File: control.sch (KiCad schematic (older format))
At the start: 1 part, among them J4 ProMicro

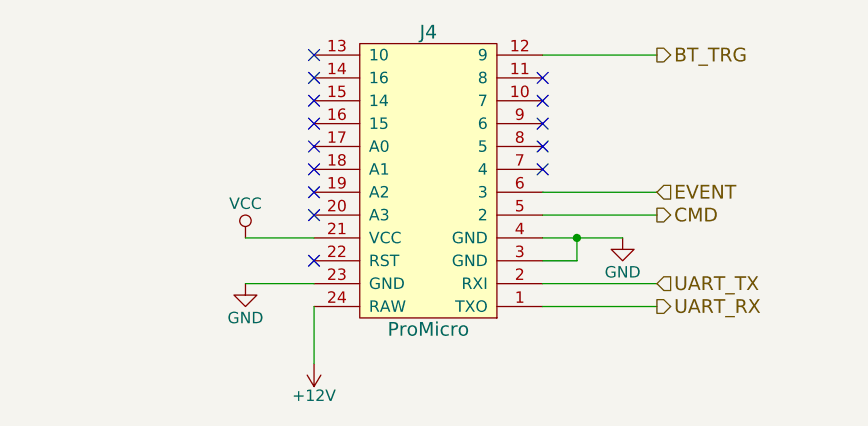
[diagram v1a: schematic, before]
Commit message: Add a ProMini part, and genericize wiring to work with either.
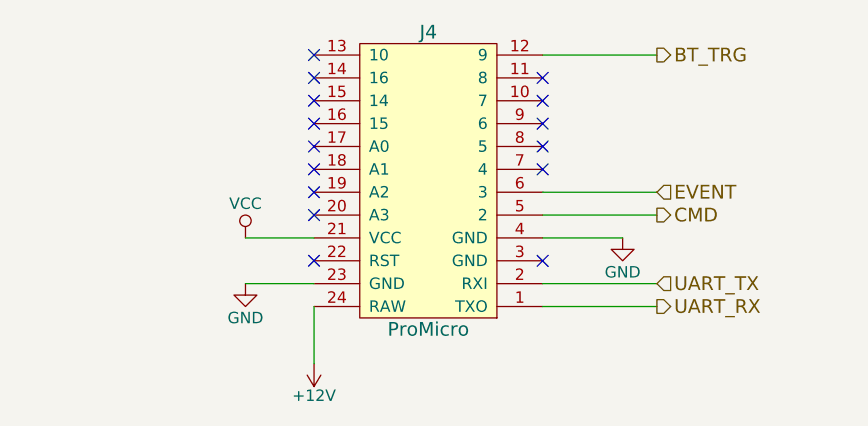
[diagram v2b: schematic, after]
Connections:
- net GND: no longer J4.3 (GND)
- no-connect marks 14 -> 15
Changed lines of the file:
@@
 	6050 4200 6400 4200
-Wire Wire Line
-	6050 4300 6200 4300
-Wire Wire Line
-	6200 4300 6200 4200
-Connection ~ 6200 4200
 Wire Wire Line
 	4750 4400 5050 4400
@@
 Wire Wire Line
 	6050 3400 6550 3400
+NoConn ~ 6050 4300
 $EndSCHEMATC

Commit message: Add LEDs to MCU and polarized caps on line driver.
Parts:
- added D2: R LED, symbol LED
- added D3: G LED, symbol LED
- added D4: BL LED, symbol LED
- added R2, R3, R4: R, symbol R
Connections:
- net BT_TRG: now also R4.2
- net GND: now also D2.1 (K), D3.1 (K), D4.1 (K)
- net VCC: now also R2.1
- net at J4.13 (10): now also R3.1
- new net: D2.2 (A), R2.2
- new net: D4.2 (A), R4.1
- new net: D3.2 (A), R3.2
- no-connect marks 15 -> 14
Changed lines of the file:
@@
 $EndComp
 $Comp
-L GND #PWR014
+L GND #PWR17
 U 1 1 589BF3A5
 P 6400 4200
-F 0 "#PWR014" H 6400 3950 50  0001 C CNN
+F 0 "#PWR17" H 6400 3950 50  0001 C CNN
 F 1 "GND" H 6400 4050 50  0000 C CNN
 F 2 "" H 6400 4200 50  0000 C CNN
@@
 $EndComp
 $Comp
-L GND #PWR015
+L GND #PWR14
 U 1 1 589BF4DD
 P 4750 4400
-F 0 "#PWR015" H 4750 4150 50  0001 C CNN
+F 0 "#PWR14" H 4750 4150 50  0001 C CNN
 F 1 "GND" H 4750 4250 50  0000 C CNN
 F 2 "" H 4750 4400 50  0000 C CNN
@@
 $EndComp
 $Comp
-L VCC #PWR016
+L VCC #PWR15
 U 1 1 589BF5FE
-P 4750 4200
-F 0 "#PWR016" H 4750 4050 50  0001 C CNN
-F 1 "VCC" H 4750 4350 50  0000 C CNN
-F 2 "" H 4750 4200 50  0000 C CNN
-F 3 "" H 4750 4200 50  0000 C CNN
-	1    4750 4200
-	1    0    0    -1
-$EndComp
-NoConn ~ 5050 3400
+P 4850 4150
+F 0 "#PWR15" H 4850 4000 50  0001 C CNN
+F 1 "VCC" H 4850 4300 50  0000 C CNN
+F 2 "" H 4850 4150 50  0000 C CNN
+F 3 "" H 4850 4150 50  0000 C CNN
+	1    4850 4150
+	1    0    0    -1
+$EndComp
 NoConn ~ 5050 3500
 NoConn ~ 5050 3600
@@
 	4750 4400 5050 4400
 Wire Wire Line
-	4750 4200 5050 4200
+	4700 4200 5050 4200
 Wire Wire Line
 	5050 4750 5050 4500
@@
 	6050 4400 6550 4400
 $Comp
-L +12V #PWR017
+L +12V #PWR16
 U 1 1 58B175C7
 P 5050 4750
-F 0 "#PWR017" H 5050 4600 50  0001 C CNN
+F 0 "#PWR16" H 5050 4600 50  0001 C CNN
 F 1 "+12V" H 5050 4890 50  0000 C CNN
 F 2 "" H 5050 4750 50  0000 C CNN
@@
 	6050 3400 6550 3400
 NoConn ~ 6050 4300
+$Comp
+L LED D2
+U 1 1 5938577D
+P 4200 4200
+F 0 "D2" H 4200 4300 50  0000 C CNN
+F 1 "R LED" H 4200 4100 50  0000 C CNN
+F 2 "" H 4200 4200 50  0001 C CNN
+F 3 "" H 4200 4200 50  0001 C CNN
+	1    4200 4200
+	1    0    0    -1
+$EndComp
+$Comp
+L LED D4
+U 1 1 593857DA
+P 7050 3550
+F 0 "D4" H 7050 3650 50  0000 C CNN
+F 1 "BL LED" H 7050 3450 50  0000 C CNN
+F 2 "" H 7050 3550 50  0001 C CNN
+F 3 "" H 7050 3550 50  0001 C CNN
+	1    7050 3550
+	-1   0    0    1
+$EndComp
+$Comp
+L LED D3
+U 1 1 59385827
+P 4500 3400
+F 0 "D3" H 4500 3500 50  0000 C CNN
+F 1 "G LED" H 4500 3300 50  0000 C CNN
+F 2 "" H 4500 3400 50  0001 C CNN
+F 3 "" H 4500 3400 50  0001 C CNN
+	1    4500 3400
+	1    0    0    -1
+$EndComp
+$Comp
+L R R3
+U 1 1 5939E4C5
+P 4850 3400
+F 0 "R3" V 4930 3400 50  0000 C CNN
+F 1 "R" V 4850 3400 50  0000 C CNN
+F 2 "" V 4780 3400 50  0001 C CNN
+F 3 "" H 4850 3400 50  0001 C CNN
+	1    4850 3400
+	0    1    1    0
+$EndComp
+$Comp
+L R R2
+U 1 1 5939E53A
+P 4550 4200
+F 0 "R2" V 4630 4200 50  0000 C CNN
+F 1 "R" V 4550 4200 50  0000 C CNN
+F 2 "" V 4480 4200 50  0001 C CNN
+F 3 "" H 4550 4200 50  0001 C CNN
+	1    4550 4200
+	0    1    1    0
+$EndComp
+$Comp
+L R R4
+U 1 1 5939E58C
+P 6700 3550
+F 0 "R4" V 6780 3550 50  0000 C CNN
+F 1 "R" V 6700 3550 50  0000 C CNN
+F 2 "" V 6630 3550 50  0001 C CNN
+F 3 "" H 6700 3550 50  0001 C CNN
+	1    6700 3550
+	0    1    1    0
+$EndComp
+$Comp
+L GND #PWR18
+U 1 1 5939E7BC
+P 7300 3600
+F 0 "#PWR18" H 7300 3350 50  0001 C CNN
+F 1 "GND" H 7300 3450 50  0000 C CNN
+F 2 "" H 7300 3600 50  0001 C CNN
+F 3 "" H 7300 3600 50  0001 C CNN
+	1    7300 3600
+	1    0    0    -1
+$EndComp
+$Comp
+L GND #PWR13
+U 1 1 5939E808
+P 4150 3450
+F 0 "#PWR13" H 4150 3200 50  0001 C CNN
+F 1 "GND" H 4150 3300 50  0000 C CNN
+F 2 "" H 4150 3450 50  0001 C CNN
+F 3 "" H 4150 3450 50  0001 C CNN
+	1    4150 3450
+	1    0    0    -1
+$EndComp
+$Comp
+L GND #PWR12
+U 1 1 5939E82E
+P 3850 4250
+F 0 "#PWR12" H 3850 4000 50  0001 C CNN
+F 1 "GND" H 3850 4100 50  0000 C CNN
+F 2 "" H 3850 4250 50  0001 C CNN
+F 3 "" H 3850 4250 50  0001 C CNN
+	1    3850 4250
+	1    0    0    -1
+$EndComp
+Wire Wire Line
+	6450 3400 6450 3550
+Wire Wire Line
+	6450 3550 6550 3550
+Connection ~ 6450 3400
+Wire Wire Line
+	6850 3550 6900 3550
+Wire Wire Line
+	7200 3550 7300 3550
+Wire Wire Line
+	7300 3550 7300 3600
+Wire Wire Line
+	5050 3400 5000 3400
+Wire Wire Line
+	4700 3400 4650 3400
+Wire Wire Line
+	4350 3400 4150 3400
+Wire Wire Line
+	4150 3400 4150 3450
+Wire Wire Line
+	4400 4200 4350 4200
+Wire Wire Line
+	4050 4200 3850 4200
+Wire Wire Line
+	3850 4200 3850 4250
+Wire Wire Line
+	4850 4150 4850 4200
+Connection ~ 4850 4200
 $EndSCHEMATC

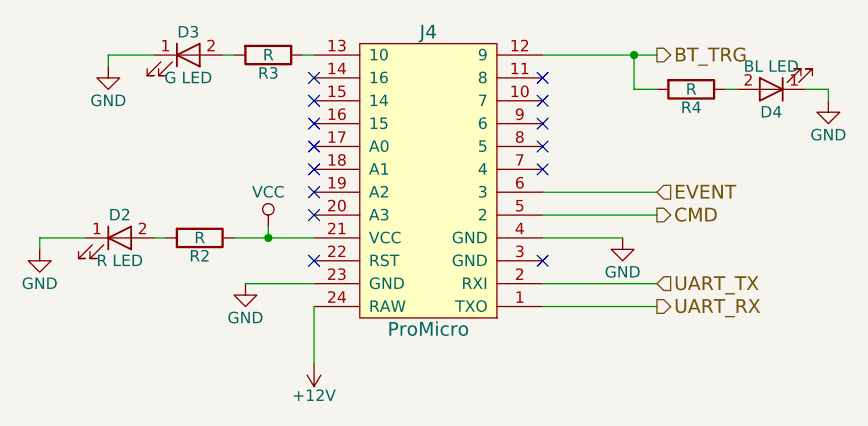
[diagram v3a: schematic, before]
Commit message: Add resistor values to LEDs and a voltage regulator. Has power pin errors still.
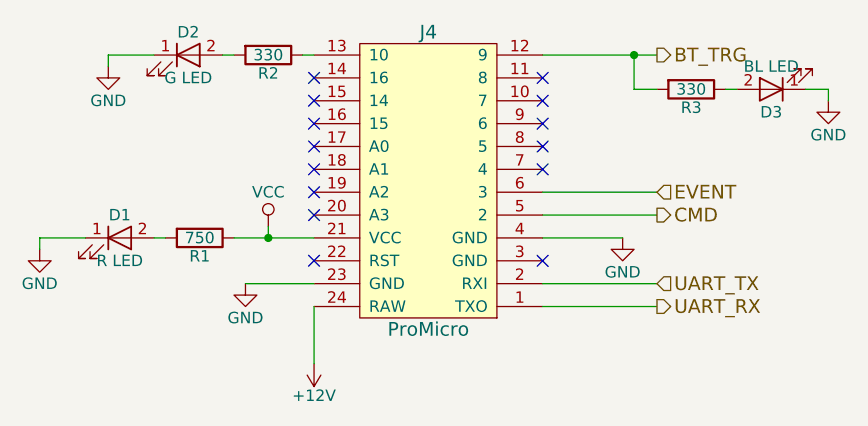
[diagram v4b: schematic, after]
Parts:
- R1: renamed from R2; value R -> 750
- R2: renamed from R3; value R -> 330
- R3: renamed from R4; value R -> 330
- renumbered D2 to D1, D3 to D2, D4 to D3
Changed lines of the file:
@@
 $EndComp
 $Comp
-L GND #PWR17
+L GND #PWR016
 U 1 1 589BF3A5
 P 6400 4200
-F 0 "#PWR17" H 6400 3950 50  0001 C CNN
+F 0 "#PWR016" H 6400 3950 50  0001 C CNN
 F 1 "GND" H 6400 4050 50  0000 C CNN
 F 2 "" H 6400 4200 50  0000 C CNN
@@
 $EndComp
 $Comp
-L GND #PWR14
+L GND #PWR017
 U 1 1 589BF4DD
 P 4750 4400
-F 0 "#PWR14" H 4750 4150 50  0001 C CNN
+F 0 "#PWR017" H 4750 4150 50  0001 C CNN
 F 1 "GND" H 4750 4250 50  0000 C CNN
 F 2 "" H 4750 4400 50  0000 C CNN
@@
 $EndComp
 $Comp
-L VCC #PWR15
+L VCC #PWR018
 U 1 1 589BF5FE
 P 4850 4150
-F 0 "#PWR15" H 4850 4000 50  0001 C CNN
+F 0 "#PWR018" H 4850 4000 50  0001 C CNN
 F 1 "VCC" H 4850 4300 50  0000 C CNN
 F 2 "" H 4850 4150 50  0000 C CNN
@@
 	6050 4400 6550 4400
 $Comp
-L +12V #PWR16
+L +12V #PWR019
 U 1 1 58B175C7
 P 5050 4750
-F 0 "#PWR16" H 5050 4600 50  0001 C CNN
+F 0 "#PWR019" H 5050 4600 50  0001 C CNN
 F 1 "+12V" H 5050 4890 50  0000 C CNN
 F 2 "" H 5050 4750 50  0000 C CNN
@@
 NoConn ~ 6050 4300
 $Comp
-L LED D2
+L LED D1
 U 1 1 5938577D
 P 4200 4200
-F 0 "D2" H 4200 4300 50  0000 C CNN
+F 0 "D1" H 4200 4300 50  0000 C CNN
 F 1 "R LED" H 4200 4100 50  0000 C CNN
 F 2 "" H 4200 4200 50  0001 C CNN
@@
 $EndComp
 $Comp
-L LED D4
+L LED D3
 U 1 1 593857DA
 P 7050 3550
-F 0 "D4" H 7050 3650 50  0000 C CNN
+F 0 "D3" H 7050 3650 50  0000 C CNN
 F 1 "BL LED" H 7050 3450 50  0000 C CNN
 F 2 "" H 7050 3550 50  0001 C CNN
@@
 $EndComp
 $Comp
-L LED D3
+L LED D2
 U 1 1 59385827
 P 4500 3400
-F 0 "D3" H 4500 3500 50  0000 C CNN
+F 0 "D2" H 4500 3500 50  0000 C CNN
 F 1 "G LED" H 4500 3300 50  0000 C CNN
 F 2 "" H 4500 3400 50  0001 C CNN
@@
 $EndComp
 $Comp
-L R R3
+L R R2
 U 1 1 5939E4C5
 P 4850 3400
-F 0 "R3" V 4930 3400 50  0000 C CNN
-F 1 "R" V 4850 3400 50  0000 C CNN
+F 0 "R2" V 4930 3400 50  0000 C CNN
+F 1 "330" V 4850 3400 50  0000 C CNN
 F 2 "" V 4780 3400 50  0001 C CNN
 F 3 "" H 4850 3400 50  0001 C CNN
@@
 $EndComp
 $Comp
-L R R2
+L R R1
 U 1 1 5939E53A
 P 4550 4200
-F 0 "R2" V 4630 4200 50  0000 C CNN
-F 1 "R" V 4550 4200 50  0000 C CNN
+F 0 "R1" V 4630 4200 50  0000 C CNN
+F 1 "750" V 4550 4200 50  0000 C CNN
 F 2 "" V 4480 4200 50  0001 C CNN
 F 3 "" H 4550 4200 50  0001 C CNN
@@
 $EndComp
 $Comp
-L R R4
+L R R3
 U 1 1 5939E58C
 P 6700 3550
-F 0 "R4" V 6780 3550 50  0000 C CNN
-F 1 "R" V 6700 3550 50  0000 C CNN
+F 0 "R3" V 6780 3550 50  0000 C CNN
+F 1 "330" V 6700 3550 50  0000 C CNN
 F 2 "" V 6630 3550 50  0001 C CNN
 F 3 "" H 6700 3550 50  0001 C CNN
@@
 $EndComp
 $Comp
-L GND #PWR18
+L GND #PWR020
 U 1 1 5939E7BC
 P 7300 3600
-F 0 "#PWR18" H 7300 3350 50  0001 C CNN
+F 0 "#PWR020" H 7300 3350 50  0001 C CNN
 F 1 "GND" H 7300 3450 50  0000 C CNN
 F 2 "" H 7300 3600 50  0001 C CNN
@@
 $EndComp
 $Comp
-L GND #PWR13
+L GND #PWR021
 U 1 1 5939E808
 P 4150 3450
-F 0 "#PWR13" H 4150 3200 50  0001 C CNN
+F 0 "#PWR021" H 4150 3200 50  0001 C CNN
 F 1 "GND" H 4150 3300 50  0000 C CNN
 F 2 "" H 4150 3450 50  0001 C CNN
@@
 $EndComp
 $Comp
-L GND #PWR12
+L GND #PWR022
 U 1 1 5939E82E
 P 3850 4250
-F 0 "#PWR12" H 3850 4000 50  0001 C CNN
+F 0 "#PWR022" H 3850 4000 50  0001 C CNN
 F 1 "GND" H 3850 4100 50  0000 C CNN
 F 2 "" H 3850 4250 50  0001 C CNN

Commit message: Voltage regulator adjustments and tidying
Switch to LD1117 component and add decoupling caps.
Add a decoupling cap to the audio switch
Shift some status LEDs to modules layer
Use ProMini instead of ProMicro
Update BOM
Update netlist
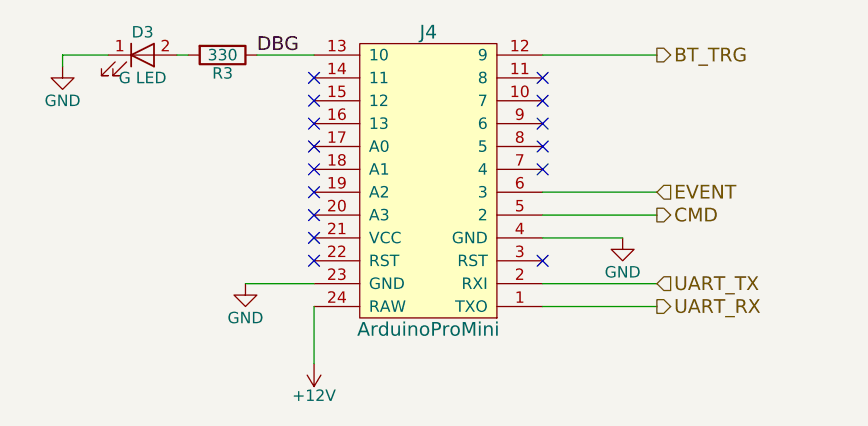
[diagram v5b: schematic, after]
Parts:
- removed D1: R LED, symbol LED
- removed D3: BL LED, symbol LED
- removed J4: ProMicro, blubaru:ProMicro, symbol ProMicro
- removed R1: 750, symbol R
- removed R3: 330, symbol R
- added J4: ArduinoProMini, blubaru:ProMicro, symbol ArduinoProMini
- D3: renamed from D2; footprint (none) -> LEDs:LED_D3.0mm_Horizontal_O1.27mm_Z2.0mm
- R3: renamed from R2; footprint (none) -> Resistors_THT:R_Axial_DIN0204_L3.6mm_D1.6mm_P1.90mm_Vertical
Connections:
- net +12V: now also J4.24 (RAW)
- net BT_TRG: now also J4.12 (9)
- net CMD: now also J4.5 (2)
- net EVENT: now also J4.6 (3)
- net GND: now also J4.23 (GND), J4.4 (GND)
- net UART_RX: now also J4.1 (TXO)
- net UART_TX: now also J4.2 (RXI)
- net DBG: now reaches R3.1
- net DBG: now also J4.13 (10)
- no-connect marks 14 -> 15
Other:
- moved on the sheet: D3, R3
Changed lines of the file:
@@
 $EndDescr
 $Comp
-L ProMicro J4
-U 1 1 589BEE21
-P 5550 4600
-F 0 "J4" H 5550 3300 60  0000 C CNN
-F 1 "ProMicro" H 5550 4600 60  0000 C CNN
-F 2 "blubaru:ProMicro" H 5550 4600 60  0001 C CNN
-F 3 "https://cdn.sparkfun.com/datasheets/Dev/Arduino/Boards/ProMicro8MHzv1.pdf" H 5550 4600 60  0001 C CNN
-	1    5550 4600
-	-1   0    0    1
-$EndComp
-$Comp
-L GND #PWR016
+L GND #PWR018
 U 1 1 589BF3A5
 P 6400 4200
-F 0 "#PWR016" H 6400 3950 50  0001 C CNN
+F 0 "#PWR018" H 6400 3950 50  0001 C CNN
 F 1 "GND" H 6400 4050 50  0000 C CNN
 F 2 "" H 6400 4200 50  0000 C CNN
@@
 $EndComp
 $Comp
-L GND #PWR017
+L GND #PWR019
 U 1 1 589BF4DD
 P 4750 4400
-F 0 "#PWR017" H 4750 4150 50  0001 C CNN
+F 0 "#PWR019" H 4750 4150 50  0001 C CNN
 F 1 "GND" H 4750 4250 50  0000 C CNN
 F 2 "" H 4750 4400 50  0000 C CNN
 F 3 "" H 4750 4400 50  0000 C CNN
 	1    4750 4400
-	1    0    0    -1
-$EndComp
-$Comp
-L VCC #PWR018
-U 1 1 589BF5FE
-P 4850 4150
-F 0 "#PWR018" H 4850 4000 50  0001 C CNN
-F 1 "VCC" H 4850 4300 50  0000 C CNN
-F 2 "" H 4850 4150 50  0000 C CNN
-F 3 "" H 4850 4150 50  0000 C CNN
-	1    4850 4150
 	1    0    0    -1
 $EndComp
@@
 	4750 4400 5050 4400
 Wire Wire Line
-	4700 4200 5050 4200
-Wire Wire Line
 	5050 4750 5050 4500
 Wire Wire Line
@@
 	6050 4400 6550 4400
 $Comp
-L +12V #PWR019
+L +12V #PWR020
 U 1 1 58B175C7
 P 5050 4750
-F 0 "#PWR019" H 5050 4600 50  0001 C CNN
+F 0 "#PWR020" H 5050 4600 50  0001 C CNN
 F 1 "+12V" H 5050 4890 50  0000 C CNN
 F 2 "" H 5050 4750 50  0000 C CNN
@@
 NoConn ~ 6050 4300
 $Comp
-L LED D1
-U 1 1 5938577D
-P 4200 4200
-F 0 "D1" H 4200 4300 50  0000 C CNN
-F 1 "R LED" H 4200 4100 50  0000 C CNN
-F 2 "" H 4200 4200 50  0001 C CNN
-F 3 "" H 4200 4200 50  0001 C CNN
-	1    4200 4200
+L LED D3
+U 1 1 59385827
+P 4300 3400
+F 0 "D3" H 4300 3500 50  0000 C CNN
+F 1 "G LED" H 4300 3300 50  0000 C CNN
+F 2 "LEDs:LED_D3.0mm_Horizontal_O1.27mm_Z2.0mm" H 4300 3400 50  0001 C CNN
+F 3 "" H 4300 3400 50  0001 C CNN
+	1    4300 3400
 	1    0    0    -1
 $EndComp
 $Comp
-L LED D3
-U 1 1 593857DA
-P 7050 3550
-F 0 "D3" H 7050 3650 50  0000 C CNN
-F 1 "BL LED" H 7050 3450 50  0000 C CNN
-F 2 "" H 7050 3550 50  0001 C CNN
-F 3 "" H 7050 3550 50  0001 C CNN
-	1    7050 3550
-	-1   0    0    1
-$EndComp
-$Comp
-L LED D2
-U 1 1 59385827
-P 4500 3400
-F 0 "D2" H 4500 3500 50  0000 C CNN
-F 1 "G LED" H 4500 3300 50  0000 C CNN
-F 2 "" H 4500 3400 50  0001 C CNN
-F 3 "" H 4500 3400 50  0001 C CNN
-	1    4500 3400
-	1    0    0    -1
-$EndComp
-$Comp
-L R R2
+L R R3
 U 1 1 5939E4C5
-P 4850 3400
-F 0 "R2" V 4930 3400 50  0000 C CNN
-F 1 "330" V 4850 3400 50  0000 C CNN
-F 2 "" V 4780 3400 50  0001 C CNN
-F 3 "" H 4850 3400 50  0001 C CNN
-	1    4850 3400
+P 4650 3400
+F 0 "R3" V 4730 3400 50  0000 C CNN
+F 1 "330" V 4650 3400 50  0000 C CNN
+F 2 "Resistors_THT:R_Axial_DIN0204_L3.6mm_D1.6mm_P1.90mm_Vertical" V 4580 3400 50  0001 C CNN
+F 3 "" H 4650 3400 50  0001 C CNN
+	1    4650 3400
 	0    1    1    0
-$EndComp
-$Comp
-L R R1
-U 1 1 5939E53A
-P 4550 4200
-F 0 "R1" V 4630 4200 50  0000 C CNN
-F 1 "750" V 4550 4200 50  0000 C CNN
-F 2 "" V 4480 4200 50  0001 C CNN
-F 3 "" H 4550 4200 50  0001 C CNN
-	1    4550 4200
-	0    1    1    0
-$EndComp
-$Comp
-L R R3
-U 1 1 5939E58C
-P 6700 3550
-F 0 "R3" V 6780 3550 50  0000 C CNN
-F 1 "330" V 6700 3550 50  0000 C CNN
-F 2 "" V 6630 3550 50  0001 C CNN
-F 3 "" H 6700 3550 50  0001 C CNN
-	1    6700 3550
-	0    1    1    0
-$EndComp
-$Comp
-L GND #PWR020
-U 1 1 5939E7BC
-P 7300 3600
-F 0 "#PWR020" H 7300 3350 50  0001 C CNN
-F 1 "GND" H 7300 3450 50  0000 C CNN
-F 2 "" H 7300 3600 50  0001 C CNN
-F 3 "" H 7300 3600 50  0001 C CNN
-	1    7300 3600
-	1    0    0    -1
 $EndComp
 $Comp
 L GND #PWR021
 U 1 1 5939E808
-P 4150 3450
-F 0 "#PWR021" H 4150 3200 50  0001 C CNN
-F 1 "GND" H 4150 3300 50  0000 C CNN
-F 2 "" H 4150 3450 50  0001 C CNN
-F 3 "" H 4150 3450 50  0001 C CNN
-	1    4150 3450
-	1    0    0    -1
-$EndComp
-$Comp
-L GND #PWR022
-U 1 1 5939E82E
-P 3850 4250
-F 0 "#PWR022" H 3850 4000 50  0001 C CNN
-F 1 "GND" H 3850 4100 50  0000 C CNN
-F 2 "" H 3850 4250 50  0001 C CNN
-F 3 "" H 3850 4250 50  0001 C CNN
-	1    3850 4250
+P 3950 3450
+F 0 "#PWR021" H 3950 3200 50  0001 C CNN
+F 1 "GND" H 3950 3300 50  0000 C CNN
+F 2 "" H 3950 3450 50  0001 C CNN
+F 3 "" H 3950 3450 50  0001 C CNN
+	1    3950 3450
 	1    0    0    -1
 $EndComp
 Wire Wire Line
-	6450 3400 6450 3550
+	5050 3400 4800 3400
 Wire Wire Line
-	6450 3550 6550 3550
-Connection ~ 6450 3400
+	4500 3400 4450 3400
 Wire Wire Line
-	6850 3550 6900 3550
+	4150 3400 3950 3400
 Wire Wire Line
-	7200 3550 7300 3550
-Wire Wire Line
-	7300 3550 7300 3600
-Wire Wire Line
-	5050 3400 5000 3400
-Wire Wire Line
-	4700 3400 4650 3400
-Wire Wire Line
-	4350 3400 4150 3400
-Wire Wire Line
-	4150 3400 4150 3450
-Wire Wire Line
-	4400 4200 4350 4200
-Wire Wire Line
-	4050 4200 3850 4200
-Wire Wire Line
-	3850 4200 3850 4250
-Wire Wire Line
-	4850 4150 4850 4200
-Connection ~ 4850 4200
+	3950 3400 3950 3450
+$Comp
+L ArduinoProMini J4
+U 1 1 594DE4E8
+P 5550 4600
+F 0 "J4" H 5550 3300 60  0000 C CNN
+F 1 "ArduinoProMini" H 5550 4600 60  0000 C CNN
+F 2 "blubaru:ProMicro" H 5550 4600 60  0001 C CNN
+F 3 "https://cdn.sparkfun.com/datasheets/Dev/Arduino/Boards/ProMini8MHzv1.pdf" H 5550 4600 60  0001 C CNN
+	1    5550 4600
+	-1   0    0    1
+$EndComp
+NoConn ~ 5050 4200
+Text Label 4800 3400 0    60   ~ 0
+DBG
 $EndSCHEMATC
